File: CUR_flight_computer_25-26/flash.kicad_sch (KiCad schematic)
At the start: 0 parts

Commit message: Flash
Stole From Sig
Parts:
- added C20: 100n, symbol Device:C_Small
- added R10, R8, R9: 10k, symbol Device:R_Small_US
- added R11, R12, R13, R14, R15: 22, symbol Device:R_Small_US
- added U7: W25Q32JVSS, Package_SO:SOIC-8_5.3x5.3mm_P1.27mm, symbol Memory_Flash:W25Q32JVSS
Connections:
- new net: R14.2, R9.2, U7.3 (~{WP}/IO_{2})
- new net: R15.2, R8.2, U7.7 (~{HOLD}/~{RESET}/IO_{3})
- new net: R12.2, U7.5 (DI/IO_{0})
- new net: R11.2, U7.6 (CLK)
- new net: R13.2, U7.2 (DO/IO_{1})
- new net +3V3: C20.1, R10.1, R8.1, R9.1, U7.8 (VCC)
- new net FLASH RESET: R15.1
- new net FLASH_CLK: R11.1
- new net FLASH_CS: R10.2, U7.1 (~{CS})
- new net FLASH_IO0: R12.1
- new net FLASH_IO1: R13.1
- new net FLASH_IO2: R14.1
- new net GND: C20.2, U7.4 (GND)

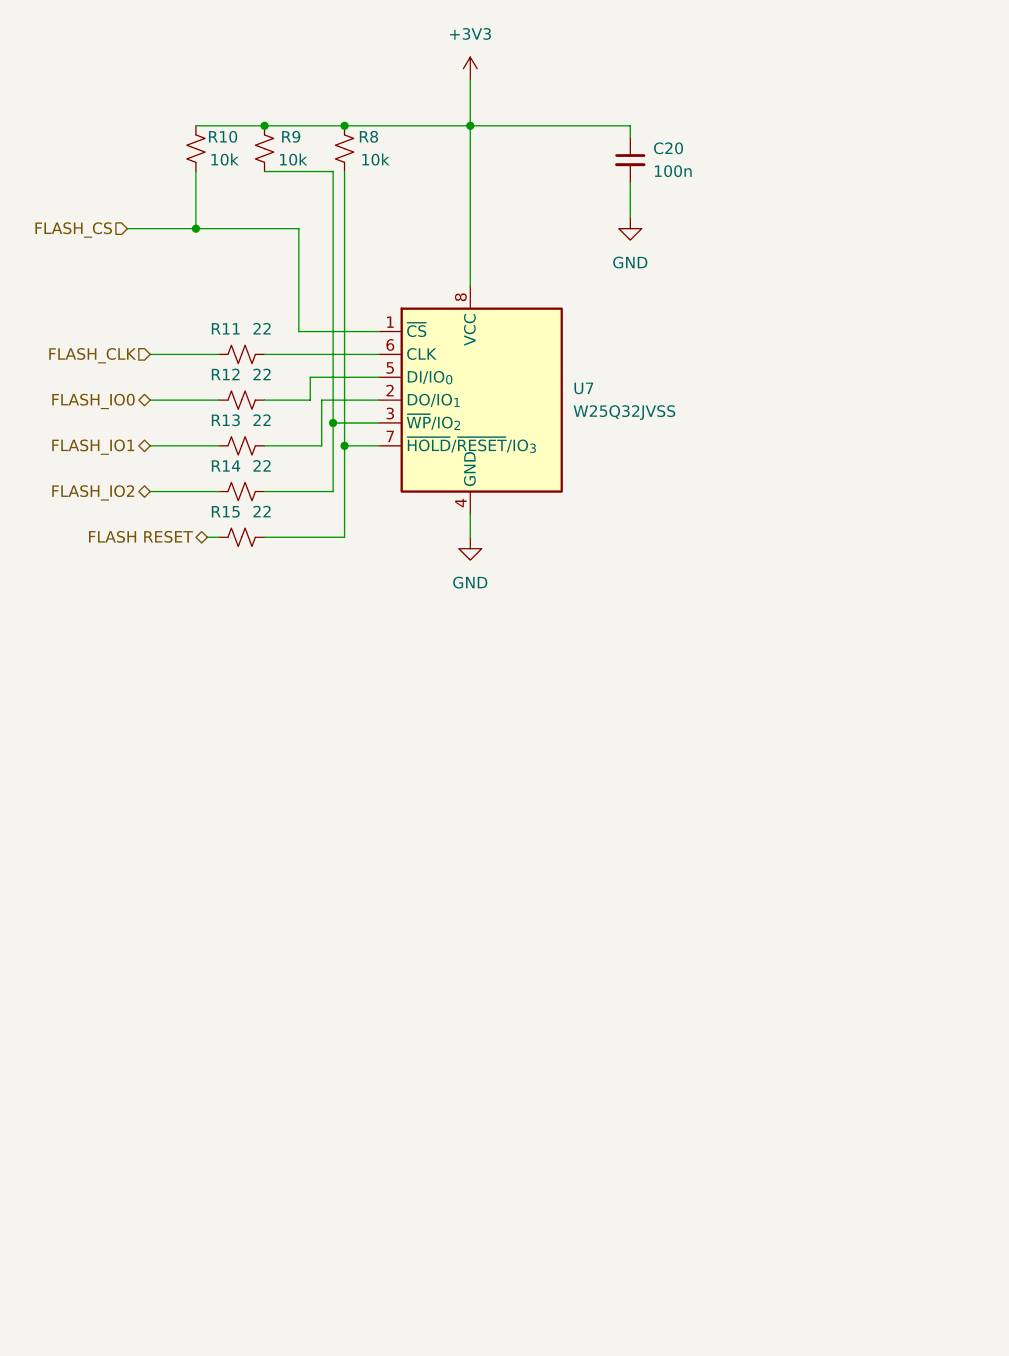
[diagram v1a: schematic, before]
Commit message: added SD_card holder
may need to confirm no pull up resistor required
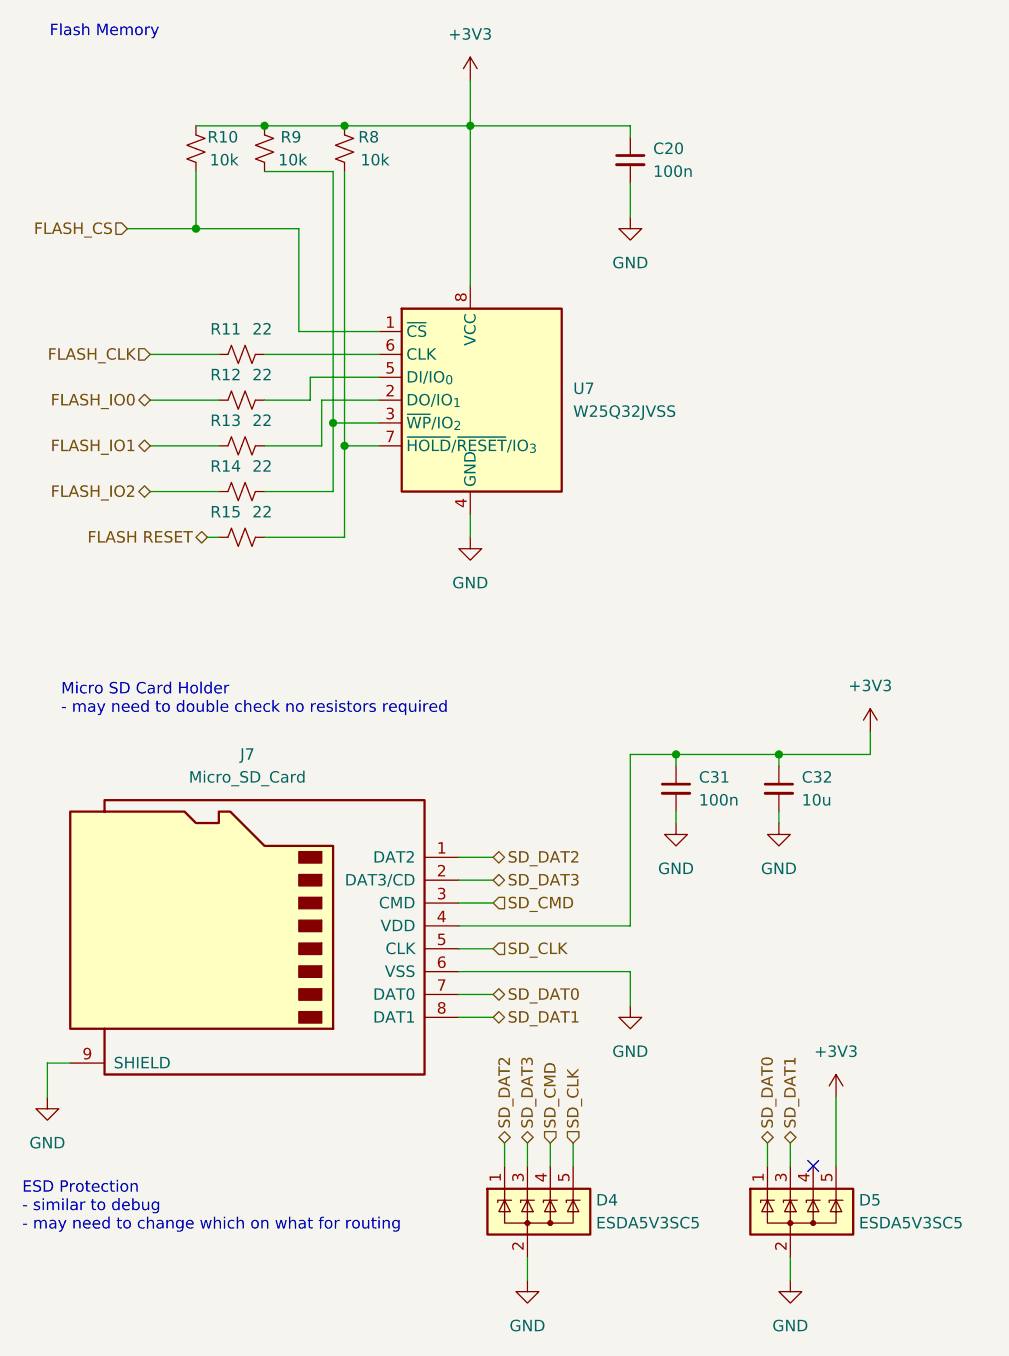
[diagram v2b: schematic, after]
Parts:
- added C31: 100n, symbol Device:C_Small
- added C32: 10u, symbol Device:C_Small
- added D4, D5: ESDA5V3SC5, Package_TO_SOT_SMD:SOT-23-5, symbol Power_Protection:ESDA5V3SC5
- added J7: Micro_SD_Card, symbol Connector:Micro_SD_Card
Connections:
- net +3V3: now also C31.1, C32.1, D5.5 (K), J7.4 (VDD)
- net GND: now also C31.2, C32.2, D4.2 (A), D5.2 (A), J7.6 (VSS), J7.9 (SHIELD)
- new net SD_CLK: D4.5 (K), J7.5 (CLK)
- new net SD_CMD: D4.4 (K), J7.3 (CMD)
- new net SD_DAT0: D5.1 (K), J7.7 (DAT0)
- new net SD_DAT1: D5.3 (K), J7.8 (DAT1)
- new net SD_DAT2: D4.1 (K), J7.1 (DAT2)
- new net SD_DAT3: D4.3 (K), J7.2 (DAT3/CD)
- no-connect marks 0 -> 1
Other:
- note added: "ESD Protection - similar to debug - may need to change which on what for routing"
- note added: "Flash Memory"
- note added: "Micro SD Card Holder - may need to double check no resistors required"

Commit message: slight pin name changes
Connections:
- net FLASH RESET renamed FLASH_IO3
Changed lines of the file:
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@@
 	(wire
 		(pts
-			(xy 35.56 78.74) (xy 36.83 78.74)
+			(xy 29.21 78.74) (xy 36.83 78.74)
 		)
 		(stroke
@@
 		)
 	)
-	(hierarchical_label "FLASH RESET"
-		(shape bidirectional)
-		(at 35.56 78.74 180)
-		(effects
-			(font
+	(hierarchical_label "FLASH_IO3"
+		(shape bidirectional)
+		(at 29.21 78.74 180)
+		(effects
+			(font

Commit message: updated all needed fixes
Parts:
- removed D4, D5: ESDA5V3SC5, Package_TO_SOT_SMD:SOT-23-5, symbol Power_Protection:ESDA5V3SC5
- added D11, D12: ESDA6V1SC5, Package_TO_SOT_SMD:SOT-23-5, symbol Power_Protection:ESDA6V1SC5
- renumbered C20 to C30, J7 to J6, R10 to R20, R11 to R21, R12 to R22, R13 to R23, R14 to R24, R15 to R25, R9 to R26, R8 to R27, U7 to U10
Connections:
- net +3V3: now also D12.5 (K)
- net GND: now also D11.2 (A), D12.2 (A)
- net SD_CLK: now also D11.5 (K)
- net SD_CMD: now also D11.4 (K)
- net SD_DAT0: now also D12.1 (K)
- net SD_DAT1: now also D12.3 (K)
- net SD_DAT2: now also D11.1 (K)
- net SD_DAT3: now also D11.3 (K)
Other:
- note added: "ESD Protection 5.25V Reverse Standoff 6V Breakdown Voltage"
- note removed: "ESD Protection - similar to debug - may need to change which on what for routing"

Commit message: assigned footrpint
need to double check:
- HSE
- Capacitors

for some unknown reason cur kicad library refuses to work
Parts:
- C30, C31, C32: footprint (none) -> Capacitor_SMD:C_0603_1608Metric
- R20, R21, R22, R23, R24, R25, R26, R27: footprint (none) -> Resistor_SMD:R_0603_1608Metric
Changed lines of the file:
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@@
 			)
 		)
-		(property "Footprint" ""
+		(property "Footprint" "Resistor_SMD:R_0603_1608Metric"
 			(at 34.29 35.56 0)
 			(effects
@@
 			)
 		)
-		(property "Footprint" ""
+		(property "Footprint" "Resistor_SMD:R_0603_1608Metric"
 			(at 39.37 73.66 0)
 			(effects
@@
 			)
 		)
-		(property "Footprint" ""
+		(property "Footprint" "Capacitor_SMD:C_0603_1608Metric"
 			(at 99.06 106.68 0)
 			(effects
@@
 			)
 		)
-		(property "Footprint" ""
+		(property "Footprint" "Capacitor_SMD:C_0603_1608Metric"
 			(at 82.55 36.83 0)
 			(effects
@@
 			)
 		)
-		(property "Footprint" ""
+		(property "Footprint" "Resistor_SMD:R_0603_1608Metric"
 			(at 50.8 35.56 0)
 			(effects
@@
 			)
 		)
-		(property "Footprint" ""
+		(property "Footprint" "Capacitor_SMD:C_0603_1608Metric"
 			(at 87.63 106.68 0)
 			(effects
@@
 			)
 		)
-		(property "Footprint" ""
+		(property "Footprint" "Resistor_SMD:R_0603_1608Metric"
 			(at 39.37 63.5 0)
 			(effects
@@
 			)
 		)
-		(property "Footprint" ""
+		(property "Footprint" "Resistor_SMD:R_0603_1608Metric"
 			(at 39.37 58.42 0)
 			(effects
@@
 			)
 		)
-		(property "Footprint" ""
+		(property "Footprint" "Resistor_SMD:R_0603_1608Metric"
 			(at 39.37 68.58 0)
 			(effects
@@
 			)
 		)
-		(property "Footprint" ""
+		(property "Footprint" "Resistor_SMD:R_0603_1608Metric"
 			(at 41.91 35.56 0)
 			(effects
@@
 			)
 		)
-		(property "Footprint" ""
+		(property "Footprint" "Resistor_SMD:R_0603_1608Metric"
 			(at 39.37 78.74 0)
 			(effects

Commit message: updated a couple footprints
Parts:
- J6: footprint (none) -> MSD-4-A:CUI_MSD-4-A
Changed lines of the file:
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@@
 			)
 		)
-		(property "Footprint" ""
+		(property "Footprint" "MSD-4-A:CUI_MSD-4-A"
 			(at 11.43 114.3 0)
 			(effects

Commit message: Revert "updated a couple footprints"
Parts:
- J6: footprint MSD-4-A:CUI_MSD-4-A -> (none)
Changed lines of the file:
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@@
 			)
 		)
-		(property "Footprint" "MSD-4-A:CUI_MSD-4-A"
+		(property "Footprint" ""
 			(at 11.43 114.3 0)
 			(effects
